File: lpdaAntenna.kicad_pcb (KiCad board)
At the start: 2 copper layers, 96 x 64 mm, 8 parts

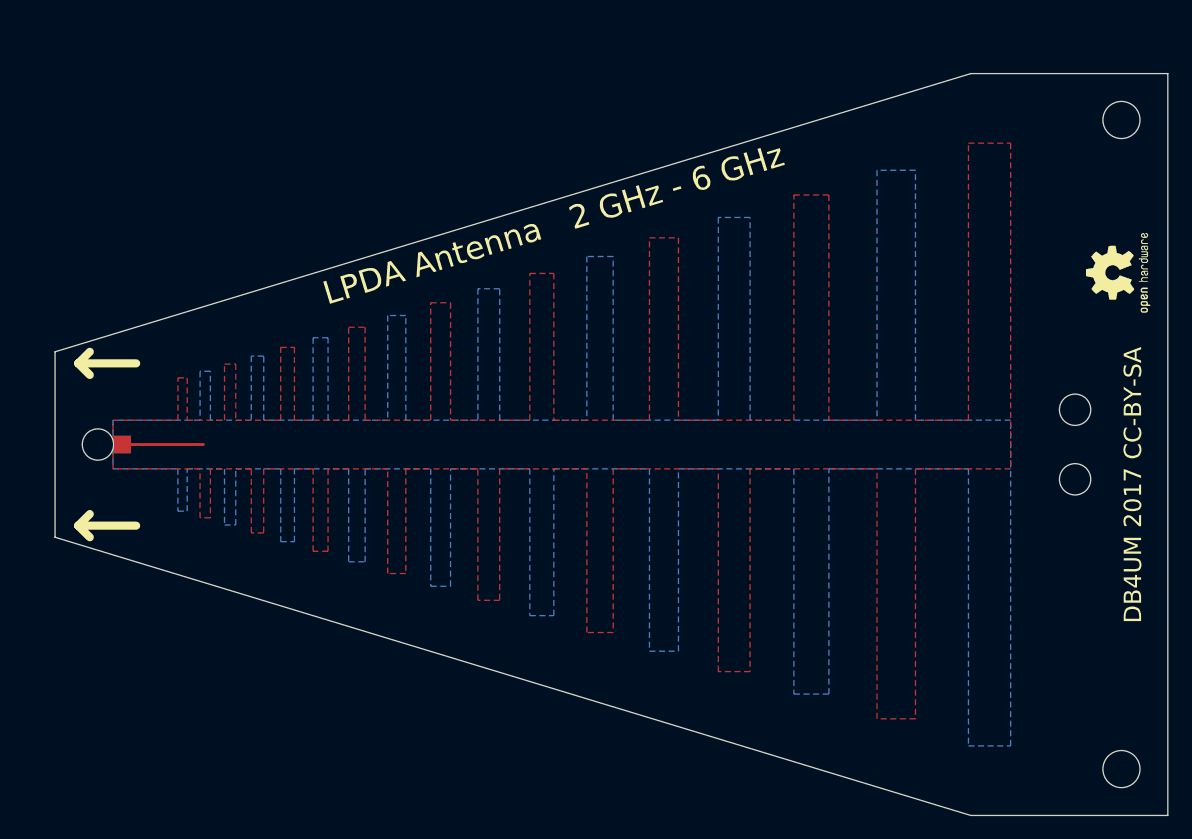
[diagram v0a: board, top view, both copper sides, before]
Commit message: nun mit pdf für Abmasse
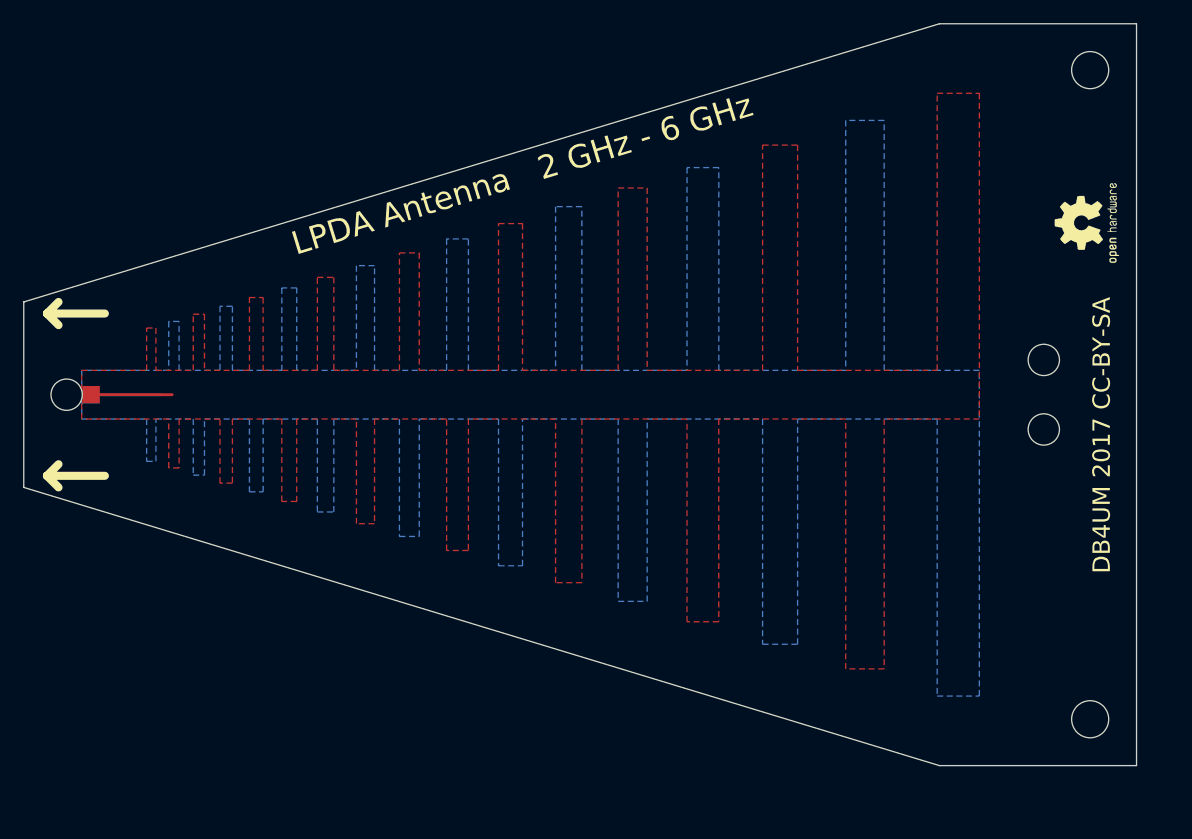
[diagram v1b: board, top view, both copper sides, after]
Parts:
- moved REF** 5.08 mm to (96.0, 95.7)
- moved TP1 5.08 mm to (98.1, 95.7)
- moved TP2 5.08 mm to (98.1, 95.7)
- moved G*** 5.08 mm to (180.3, 84.7)
- moved REF** 5.08 mm to (180.3, 98.7)
- moved REF** 5.08 mm to (184.3, 123.7)
- moved REF** 5.08 mm to (184.3, 67.7)
- moved REF** 5.08 mm to (180.3, 92.7)
